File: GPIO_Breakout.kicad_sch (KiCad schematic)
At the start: 3 parts, among them J10 Port C/D breakout, J8 Port A breakout, J9 Port B breakout

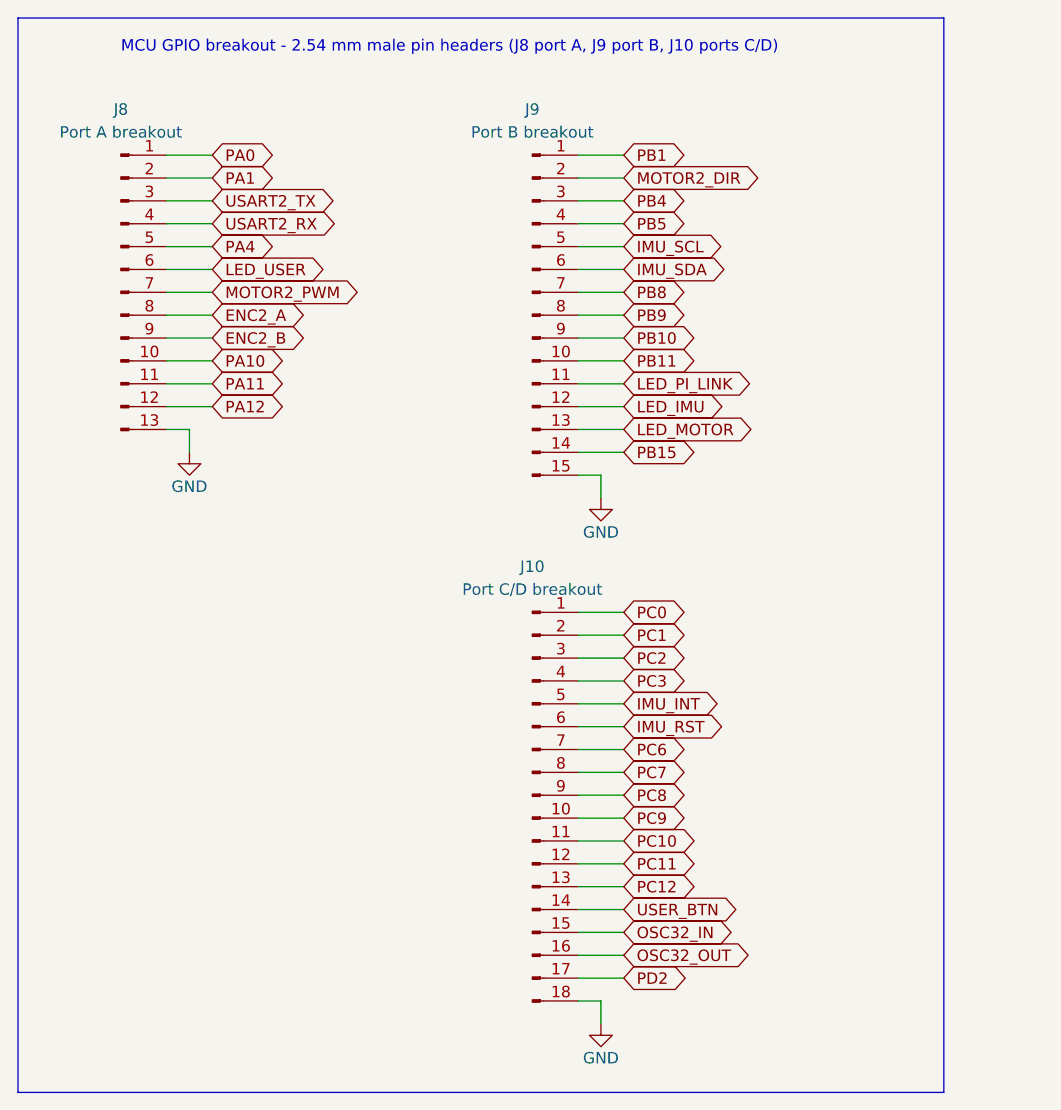
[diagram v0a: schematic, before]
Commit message: Remove the IMU from the board; it will be wired off-board
The BNO085 IMU is now connected discretely off the PCB, so everything
for it is removed from the schematic and the layout:
- Delete the IMU Interface sheet (IMU_Interface.kicad_sch): J11 STEMMA
  QT connector, J12 INT/RST header, DNP I2C pull-ups R10/R11 and series
  resistors R34/R35; remove its sheet block, note and project entry
- Remove debug LED D10 / R23 (LED_IMU on PB13)
- Rename the freed MCU nets back to plain pins, still broken out on the
  GPIO headers: IMU_SCL -> PB6, IMU_SDA -> PB7 (J9), IMU_INT -> PC4,
  IMU_RST -> PC5 (J10), LED_IMU -> PB13 (J9)
- Drop IMU wiring notes and the IMU 3.3 V budget line from the LDO sheet;
  update the J9/J10 pin descriptions, debug-LED note and README

Board updated to match (as Update PCB from Schematic): the eight
unplaced footprints deleted, pad nets renamed, J9/J10 descriptions
synced. ERC 0; DRC unchanged at 57 with 276 unrouted (was 293);
schematic parity clean.

Co-Authored-By: Claude Opus 5.5 <noreply@anthropic.com>
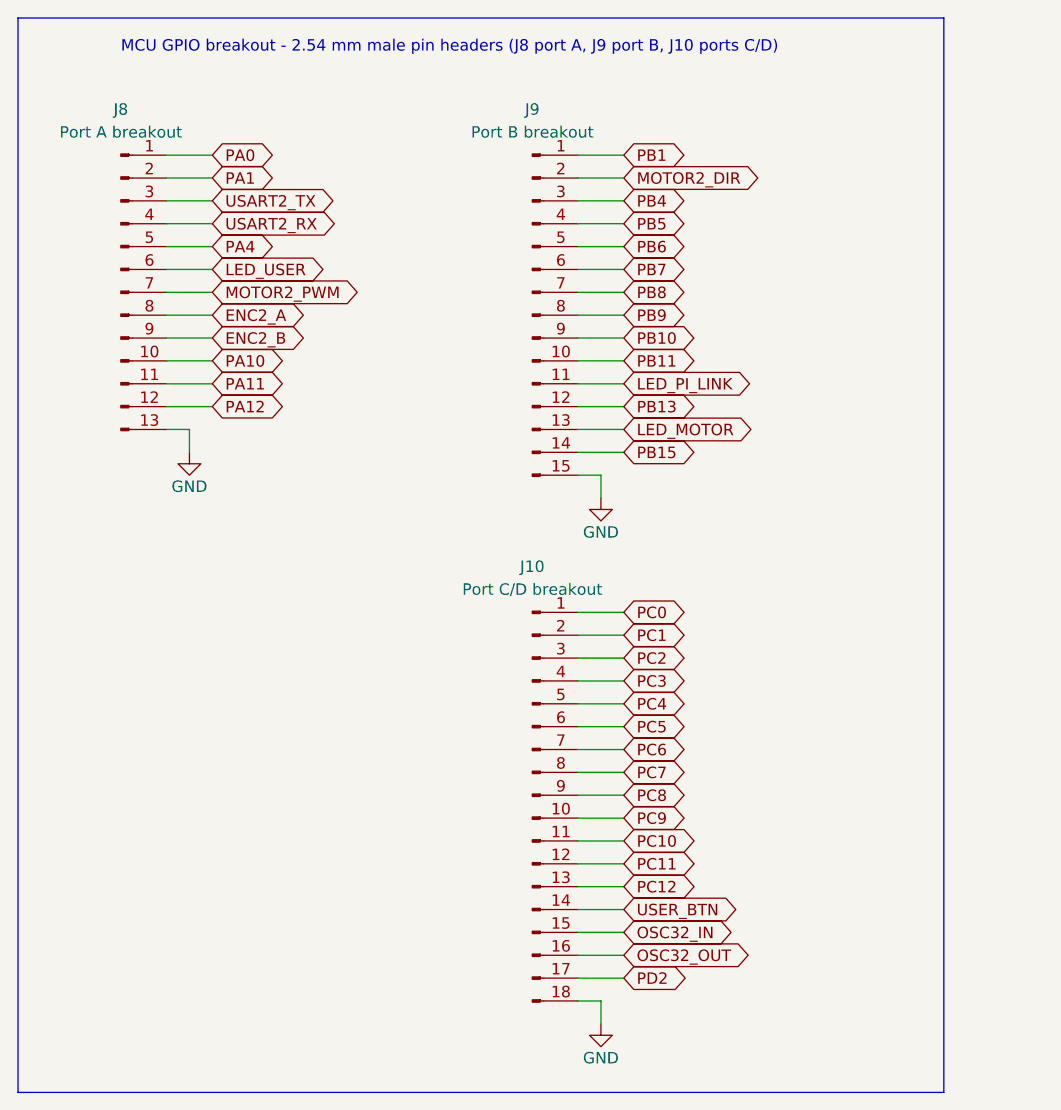
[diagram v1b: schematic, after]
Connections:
- net IMU_INT renamed PC4
- net IMU_RST renamed PC5
- net IMU_SCL renamed PB6
- net IMU_SDA renamed PB7
- net LED_IMU renamed PB13
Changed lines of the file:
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@@
 		)
 	)
-	(global_label "IMU_SCL"
+	(global_label "PB6"
 		(shape bidirectional)
 		(at 111.76 71.12 0)
@@
 		)
 	)
-	(global_label "IMU_SDA"
+	(global_label "PB7"
 		(shape bidirectional)
 		(at 111.76 73.66 0)
@@
 		)
 	)
-	(global_label "IMU_INT"
+	(global_label "PC4"
 		(shape bidirectional)
 		(at 111.76 121.92 0)
@@
 		)
 	)
-	(global_label "LED_IMU"
+	(global_label "PB13"
 		(shape bidirectional)
 		(at 111.76 88.9 0)
@@
 		)
 	)
-	(global_label "IMU_RST"
+	(global_label "PC5"
 		(shape bidirectional)
 		(at 111.76 124.46 0)
@@
 			)
 		)
-		(property "Description" "Male 2.54 mm pin header, 1x15 vertical: pins 1-14 = PB1, MOTOR2_DIR (PB2), PB4, PB5, IMU_SCL (PB6), IMU_SDA (PB7), PB8, PB9, PB10, PB11, LED_PI_LINK (PB12), LED_IMU (PB13), LED_MOTOR (PB14), PB15; pin 15 = GND"
+		(property "Description" "Male 2.54 mm pin header, 1x15 vertical: pins 1-14 = PB1, MOTOR2_DIR (PB2), PB4, PB5, PB6, PB7, PB8, PB9, PB10, PB11, LED_PI_LINK (PB12), PB13, LED_MOTOR (PB14), PB15; pin 15 = GND"
 			(at 101.6 78.74 0)
 			(hide yes)
@@
 			)
 		)
-		(property "Description" "Male 2.54 mm pin header, 1x18 vertical: pins 1-17 = PC0, PC1, PC2, PC3, IMU_INT (PC4), IMU_RST (PC5), PC6, PC7, PC8, PC9, PC10, PC11, PC12, USER_BTN, OSC32_IN, OSC32_OUT, PD2; pin 18 = GND"
+		(property "Description" "Male 2.54 mm pin header, 1x18 vertical: pins 1-17 = PC0, PC1, PC2, PC3, PC4, PC5, PC6, PC7, PC8, PC9, PC10, PC11, PC12, USER_BTN, OSC32_IN, OSC32_OUT, PD2; pin 18 = GND"
 			(at 101.6 132.08 0)
 			(hide yes)

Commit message: Add input protection, AUX ports, servo interface and Pi control
Implements the 2026-10-15 design review decisions in the schematic.
ERC 0 errors, 0 warnings.

New sheets:
- Input Protection: Q1 SQJ409EP reverse-battery P-FET after F1 (D12
  12 V gate clamp, R36), D13 SMBJ16A TVS on +12V, battery sense
  R37/R38/C37 -> VBAT_SENSE on PA0. PWR_FLAG moves to +12V.
- AUX Outputs: four +5V_AUX ports J18-J21 (JST XH 2-pin: Notecard,
  LiDAR, GNSS, IMU), each through a 1.5 A PTC (F4-F7).
- Servo Interface: J17 (GND, VBAT_SERVO via F3 5 A fuse, SERVO_SIG) for
  the Hiwonder HTS-30HS through an external 11.1-12 V buck. U8
  SN74LVC1T45 translates PB10 (USART3 half-duplex) to the 5 V bus,
  PB11 sets direction; R39-R42 pull-ups/series, D14 ESD.

Root sheet:
- F1 output is now VBAT_FUSED; C36 sits on +12V after Q1. J2-F1 net
  named VBAT_IN. F1 7.5 A -> 10 A (0297010.L).
- Y3/C5/C6 fitted (were DNP).
- PA0 -> VBAT_SENSE, PA1 -> PI_3V3_SENSE, PB10 -> SERVO_TX,
  PB11 -> SERVO_DIR. Notes updated (no more F2 / XT30-only text).

Pi 5 Interface:
- J13 -> 6-pin JST XH: TXD, RXD, GND, PI_3V3, PI_RESET, PI_BOOT0.
- PI_3V3 -> D15 -> AUX_EN (U5 enable) and R44/R45 -> PA1.
- PI_RESET -> Q2 DMN63D8L -> NRST (open drain, R46 pull-down).
- PI_BOOT0 -> R47 1k -> BOOT0, for reflashing over USART2.
- R12/R13 100R -> 1k (PA2/PA3 are TTa, 5 mA injection max).
- Remove TP2 (same net as TP1 since F2 was removed).

Buck 5V AUX: U5 EN from AUX_EN (was +12V), R43 100k pull-down, C40,
J22 force-on jumper. Buck 5V SYS: C49 100 nF at U3 VIN/GND.
U2/U5 value TPSM63606RDLR; VCC design note corrected (internal 1 uF,
must stay NC).

Motor Control (now A3):
- U9/U10 74LVC2G17 encoder buffers on +3V3; encoder series R 100R ->
  1k with C43-C46 1 nF; R48-R51 4.7k pull-ups (DNP).
- F8/F9 0.2 A PTC + C47/C48 on each encoder supply (ENC1_5V, ENC2_5V).
- J7/J15 pin order 5V, GND, A, B (matches the am-3651 plug).
- R52/R53 10k pull-downs on both PWM lines (MDD20A brakes on low).
- F10/F11 PTC in series with J6/J16 p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
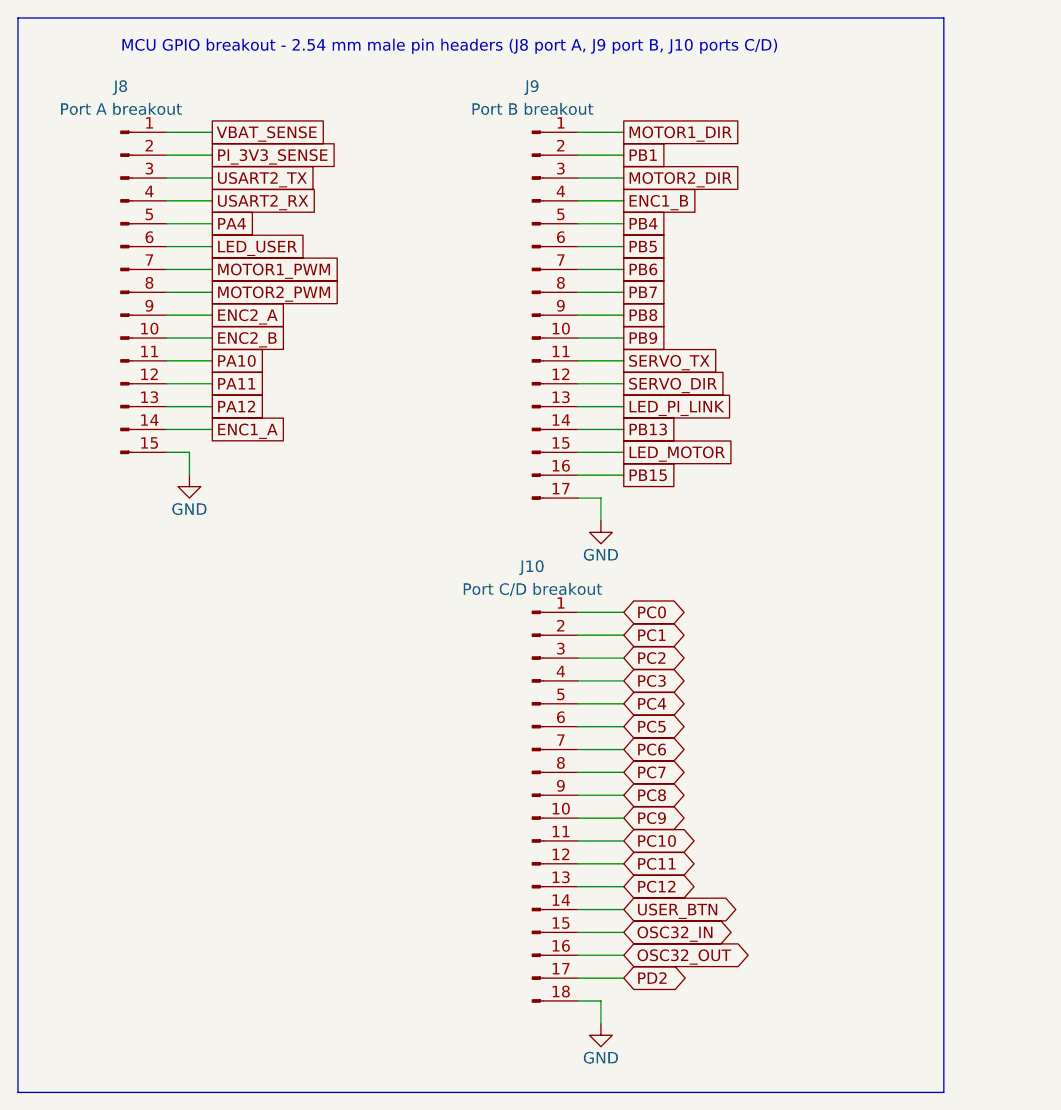
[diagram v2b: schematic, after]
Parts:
- J8: footprint Connector_PinHeader_2.54mm:PinHeader_1x13_P2.54mm_Vertical -> Connector_PinHeader_2.54mm:PinHeader_1x15_P2.54mm_Vertical; symbol Connector:Conn_01x13_Pin -> Connector:Conn_01x15_Pin
- J9: footprint Connector_PinHeader_2.54mm:PinHeader_1x15_P2.54mm_Vertical -> Connector_PinHeader_2.54mm:PinHeader_1x17_P2.54mm_Vertical; symbol Connector:Conn_01x15_Pin -> Connector:Conn_01x17_Pin
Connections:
- net PB10 is gone; now on net PB8: J9.9 (Pin_9)
- net PB11 is gone; now on net PB9: J9.10 (Pin_10)
- net ENC2_A: now also J8.9 (Pin_9); no longer J8.8 (Pin_8)
- net ENC2_B: now also J8.10 (Pin_10); no longer J8.9 (Pin_9)
- net GND: now also J8.15 (Pin_15), J9.17 (Pin_17); no longer J8.13 (Pin_13), J9.15 (Pin_15)
- net LED_MOTOR: now also J9.15 (Pin_15); no longer J9.13 (Pin_13)
- net LED_PI_LINK: now also J9.13 (Pin_13); no longer J9.11 (Pin_11)
- net MOTOR2_DIR: now also J9.3 (Pin_3); no longer J9.2 (Pin_2)
- net MOTOR2_PWM: now also J8.8 (Pin_8); no longer J8.7 (Pin_7)
- net PA10: now also J8.11 (Pin_11); no longer J8.10 (Pin_10)
- net PA11: now also J8.12 (Pin_12); no longer J8.11 (Pin_11)
- net PA12: now also J8.13 (Pin_13); no longer J8.12 (Pin_12)
- net PB1: now also J9.2 (Pin_2); no longer J9.1 (Pin_1)
- net PB13: now also J9.14 (Pin_14); no longer J9.12 (Pin_12)
- net PB15: now also J9.16 (Pin_16); no longer J9.14 (Pin_14)
- net PB4: now also J9.5 (Pin_5); no longer J9.3 (Pin_3)
- net PB5: now also J9.6 (Pin_6); no longer J9.4 (Pin_4)
- net PB6: now also J9.7 (Pin_7); no longer J9.5 (Pin_5)
- net PB7: now also J9.8 (Pin_8); no longer J9.6 (Pin_6)
- net PB8: no longer J9.7 (Pin_7)
- net PB9: no longer J9.8 (Pin_8)
- net PA0 renamed VBAT_SENSE
- net PA1 renamed PI_3V3_SENSE
- new net ENC1_A: J8.14 (Pin_14)
- new net ENC1_B: J9.4 (Pin_4)
- new net MOTOR1_DIR: J9.1 (Pin_1)
- new net MOTOR1_PWM: J8.7 (Pin_7)
- new net SERVO_DIR: J9.12 (Pin_12)
- new net SERVO_TX: J9.11 (Pin_11)
